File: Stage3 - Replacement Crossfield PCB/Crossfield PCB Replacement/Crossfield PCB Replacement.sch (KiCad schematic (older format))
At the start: 30 parts, among them P16-2 Power Amp Right, P25-2 Power Amp Left, P4-P24 Switch Mode PSU, P6-P18 12_Way_8-215079-2, Q1 BC549, Q2 BC549, Q3 BC549, Q4 BC549

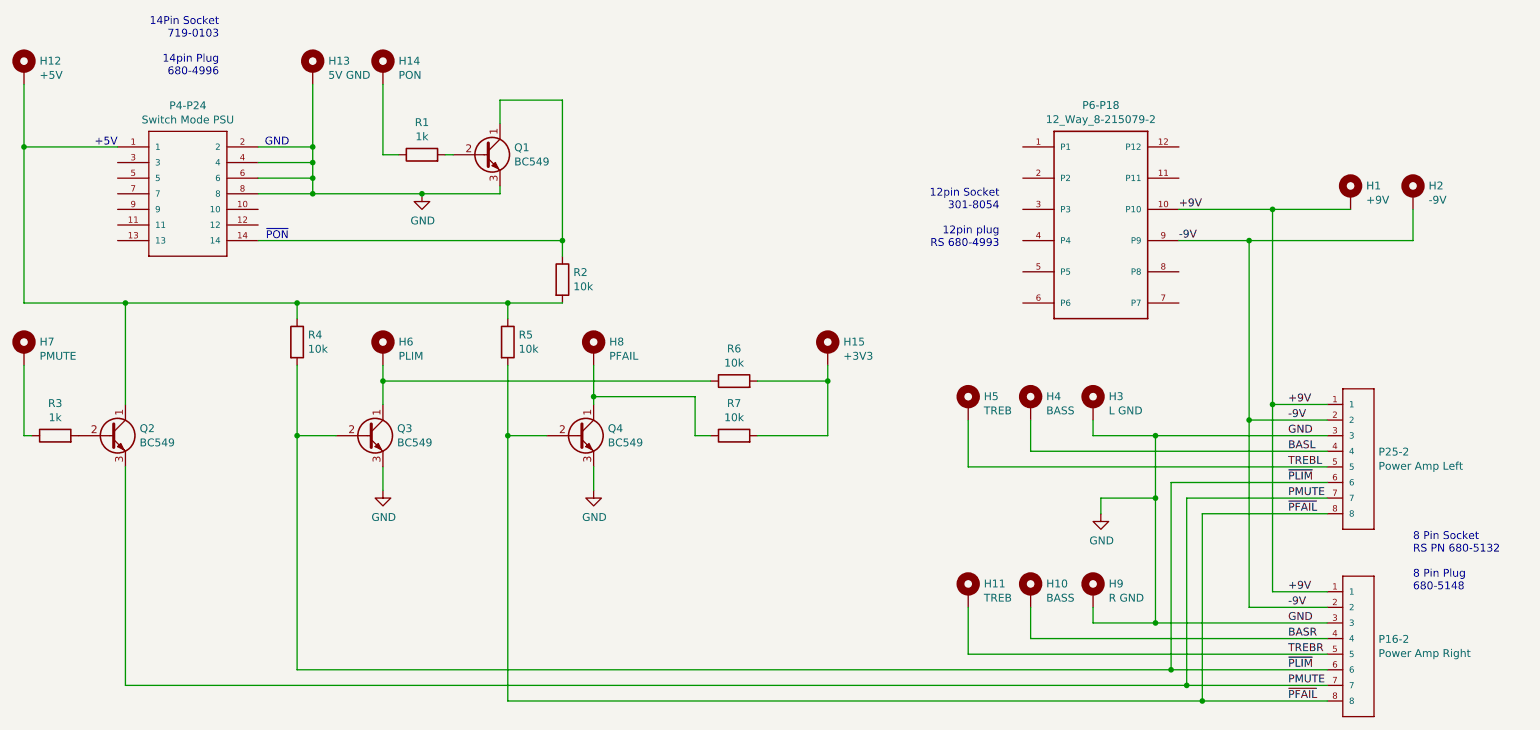
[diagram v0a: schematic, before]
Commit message: Changed PCB now has USB PSU
The B&O PSU failed to provide enough mA for the raspberry. Now the switchmode PSU has been removed and replaced with a standard USB brick.
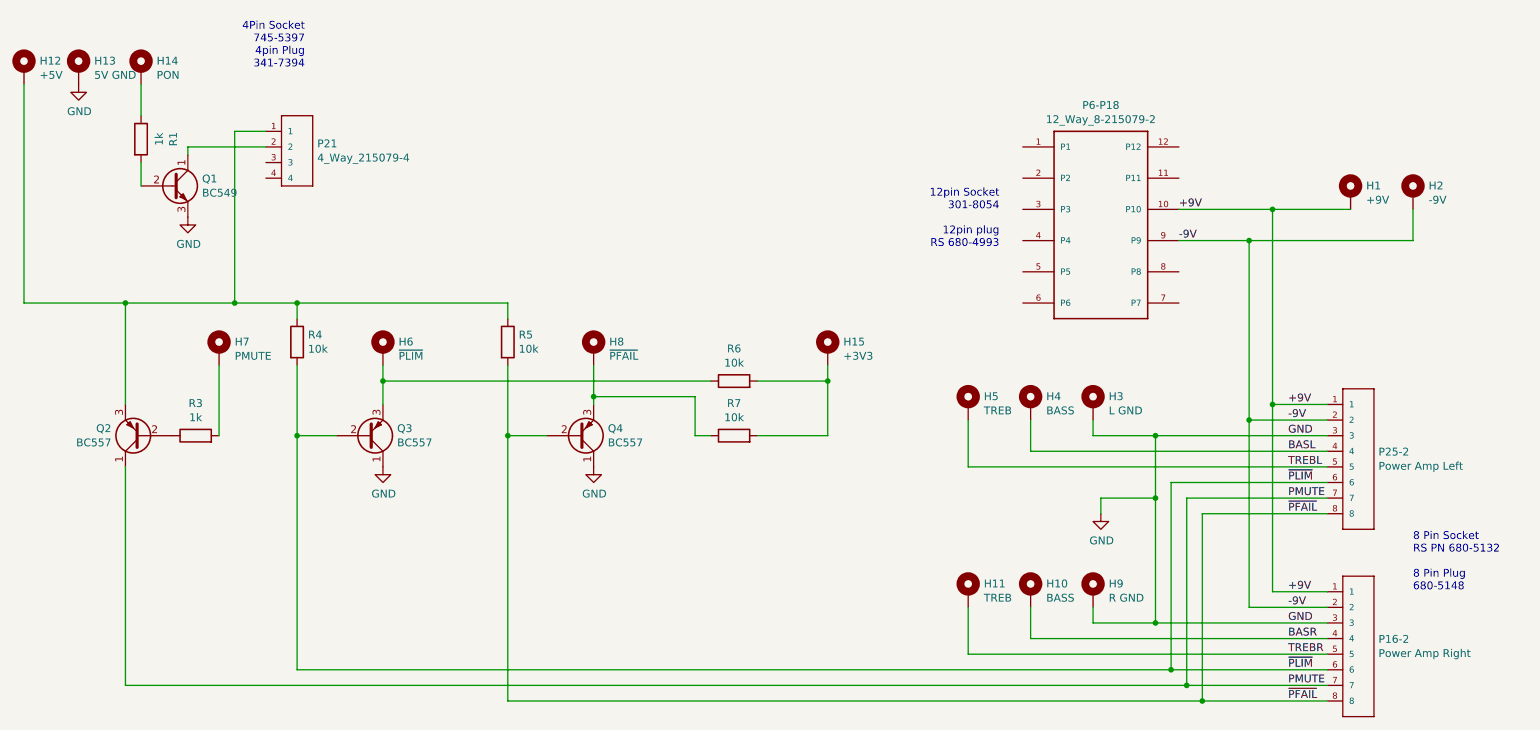
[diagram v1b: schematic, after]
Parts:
- removed P4-P24: Switch Mode PSU, TE_2-215079-0, symbol TE_Amp_215079_PCB_Sockets:14_Way_1-215079-4
- removed Q2, Q3, Q4: BC549, Package_TO_SOT_THT:TO-92_Inline, symbol Transistor_BJT:BC548
- removed R2: 10k, Resistor_THT:R_Axial_DIN0204_L3.6mm_D1.6mm_P7.62mm_Horizontal, symbol Device:R
- added P21: 4_Way_215079-4, Connector_TE_215079_Series:TE_215079-4, symbol TE_Amp_215079_PCB_Sockets:4_Way_215079-4
- added Q2, Q3, Q4: BC557, Package_TO_SOT_THT:TO-92_Inline, symbol Transistor_BJT:BC557
- H6: value PLIM -> ~PLIM
- H8: value PFAIL -> ~PFAIL
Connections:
- net GND: now also Q3.1 (C), Q4.1 (C)
- net PMUTE: now also Q2.1 (C)
- net ~PFAIL: now also Q4.2 (B)
- net ~PLIM: now also Q3.2 (B)
- net at H7.1: now also R3.2; no longer R3.1
- net at H12.1, R4.1, R5.1: now also P21.1, Q2.3 (E)
- net at Q1.1 (C): now also P21.2
- net at H6.1, R6.1: now also Q3.3 (E)
- net at H8.1, R7.1: now also Q4.3 (E)
- new net: Q2.2 (B), R3.1
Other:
- note added: "4Pin Socket\n745-5397\n4pin Plug\n341-7394"
- note removed: "+5V"
- note removed: "14Pin Socket\n719-0103\n\n14pin Plug\n680-4996"
- note removed: "GND"
- note removed: "~PON"
- moved on the sheet: H13, H14, H7, R1, R3

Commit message: Updated PCB following tests on PMUTE
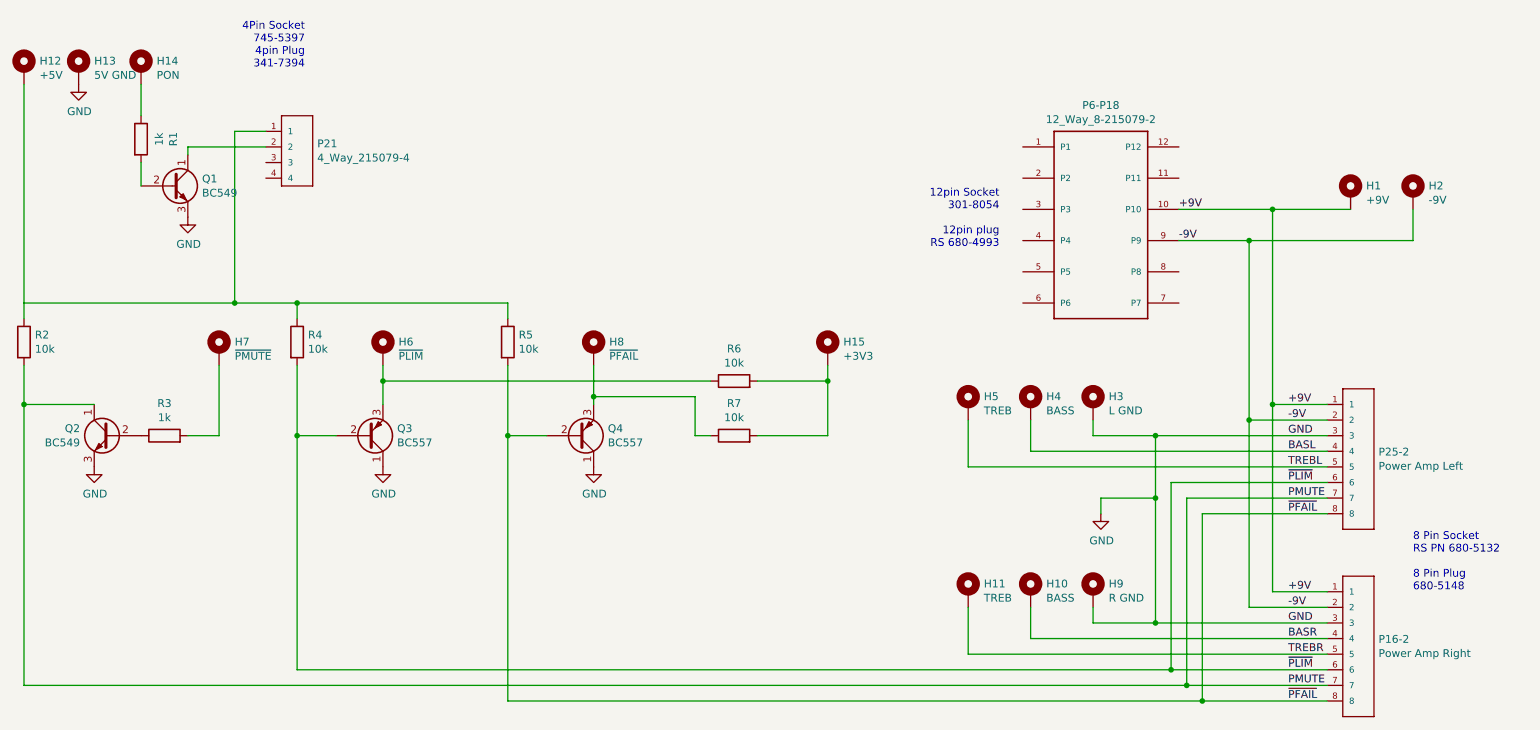
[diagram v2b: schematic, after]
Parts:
- removed Q2: BC557, Package_TO_SOT_THT:TO-92_Inline, symbol Transistor_BJT:BC557
- added Q2: BC549, Package_TO_SOT_THT:TO-92_Inline, symbol Transistor_BJT:BC548
- added R2: 10k, Resistor_THT:R_Axial_DIN0204_L3.6mm_D1.6mm_P7.62mm_Horizontal, symbol Device:R
- H7: value PMUTE -> ~PMUTE
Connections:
- net GND: now also Q2.3 (E)
- net PMUTE: now also Q2.1 (C), R2.2
- net at H12.1, P21.1, R4.1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: now also R2.1
- net at R3.1: now also Q2.2 (B)
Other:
- moved on the sheet: R3
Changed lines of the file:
@@
 P 4600 4850
 F 0 "H7" H 4700 4901 50  0000 L CNN
-F 1 "PMUTE" H 4700 4810 50  0000 L CNN
+F 1 "~PMUTE" H 4700 4810 50  0000 L CNN
 F 2 "Connector_Wire:SolderWirePad_1x01_Drill1.2mm" H 4600 4850 50  0001 C CNN
 F 3 "~" H 4600 4850 50  0001 C CNN
@@
 L Device:R R3
 U 1 1 5C7B7D41
-P 4450 5400
-F 0 "R3" V 4657 5400 50  0000 C CNN
-F 1 "1k" V 4566 5400 50  0000 C CNN
-F 2 "Resistor_THT:R_Axial_DIN0204_L3.6mm_D1.6mm_P7.62mm_Horizontal" V 4380 5400 50  0001 C CNN
-F 3 "~" H 4450 5400 50  0001 C CNN
-	1    4450 5400
+P 4250 5400
+F 0 "R3" V 4457 5400 50  0000 C CNN
+F 1 "1k" V 4366 5400 50  0000 C CNN
+F 2 "Resistor_THT:R_Axial_DIN0204_L3.6mm_D1.6mm_P7.62mm_Horizontal" V 4180 5400 50  0001 C CNN
+F 3 "~" H 4250 5400 50  0001 C CNN
+	1    4250 5400
 	0    -1   -1   0
 $EndComp
-Wire Wire Line
-	4600 4950 4600 5400
 Wire Wire Line
 	10900 5900 10900 7100
@@
 Wire Wire Line
 	10800 7000 11700 7000
-Wire Wire Line
-	4000 5600 4000 7000
-Wire Wire Line
-	4000 7000 10800 7000
 $Comp
 L power:GND #PWR0102
@@
 	1    0    0    -1
 $EndComp
-Wire Wire Line
-	4000 5200 4000 4550
 $Comp
 L Device:R R4
@@
 	4700 4550 5100 4550
 Connection ~ 5100 4550
-Wire Wire Line
-	3350 4550 4000 4550
-Wire Wire Line
-	4700 4550 4000 4550
 Connection ~ 4700 4550
-Connection ~ 4000 4550
 Wire Wire Line
 	4100 3650 4100 3800
@@
 	1    4400 4000
 	1    0    0    -1
-$EndComp
-$Comp
-L Transistor_BJT:BC557 Q2
-U 1 1 5C99A905
-P 4100 5400
-F 0 "Q2" H 4290 5354 50  0000 L CNN
-F 1 "BC557" H 4290 5445 50  0000 L CNN
-F 2 "Package_TO_SOT_THT:TO-92_Inline" H 4300 5325 50  0001 L CIN
-F 3 "http://www.fairchildsemi.com/ds/BC/BC557.pdf" H 4100 5400 50  0001 L CNN
-	1    4100 5400
-	-1   0    0    1
 $EndComp
 Wire Wire Line
@@
 	1    0    0    1
 $EndComp
+$Comp
+L Device:R R2
+U 1 1 5C9EBECA
+P 3350 4800
+F 0 "R2" H 3420 4846 50  0000 L CNN
+F 1 "10k" H 3420 4755 50  0000 L CNN
+F 2 "Resistor_THT:R_Axial_DIN0204_L3.6mm_D1.6mm_P7.62mm_Horizontal" V 3280 4800 50  0001 C CNN
+F 3 "~" H 3350 4800 50  0001 C CNN
+	1    3350 4800
+	1    0    0    -1
+$EndComp
+Wire Wire Line
+	3350 4650 3350 4550
+$Comp
+L Transistor_BJT:BC548 Q2
+U 1 1 5C9F2222
+P 3900 5400
+F 0 "Q2" H 4091 5446 50  0000 L CNN
+F 1 "BC549" H 4091 5355 50  0000 L CNN
+F 2 "Package_TO_SOT_THT:TO-92_Inline" H 4100 5325 50  0001 L CIN
+F 3 "http://www.fairchildsemi.com/ds/BC/BC547.pdf" H 3900 5400 50  0001 L CNN
+	1    3900 5400
+	-1   0    0    -1
+$EndComp
+Wire Wire Line
+	3350 7000 10800 7000
+Wire Wire Line
+	3350 4550 4700 4550
+$Comp
+L power:GND #PWR?
+U 1 1 5C9FE5CA
+P 3800 5600
+F 0 "#PWR?" H 3800 5350 50  0001 C CNN
+F 1 "GND" H 3805 5427 50  0000 C CNN
+F 2 "" H 3800 5600 50  0001 C CNN
+F 3 "" H 3800 5600 50  0001 C CNN
+	1    3800 5600
+	1    0    0    -1
+$EndComp
+Wire Wire Line
+	4400 5400 4600 5400
+Wire Wire Line
+	3350 4950 3350 5200
+Wire Wire Line
+	4600 4950 4600 5400
+Wire Wire Line
+	3800 5200 3350 5200
+Connection ~ 3350 5200
+Wire Wire Line
+	3350 5200 3350 7000
 $EndSCHEMATC
